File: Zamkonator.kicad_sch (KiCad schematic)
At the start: 27 parts, among them J1 Screw_Terminal_01x06, J3 Conn_01x08_Male, J4 Conn_02x06_Counter_Clockwise, J5 Conn_01x04_Female, J6 Conn_01x03_Female

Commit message: Switch to LCSC RJ45 socket
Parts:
- J1: LCSC (none) -> C918124
- J_LATCH1: LCSC (none) -> C918120
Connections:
- net RT9400_VA1: no longer J5.1 (Pin_1)
- net RT9400_VA2: no longer J5.2 (Pin_2)
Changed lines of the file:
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@@
-    (effects (font (size 1.27 1.27)) (justify right bottom))
-  )
-  (label "RT9400_VA2" (at 73.025 40.64 270)
     (effects (font (size 1.27 1.27)) (justify right bottom))
   )
   (label "RT9400_VA2" (at 110.49 73.66 90)
     (effects (font (size 1.27 1.27)) (justify left bottom))
-  )
-  (label "RT9400_VA1" (at 70.485 40.64 270)
-    (effects (font (size 1.27 1.27)) (justify right bottom))
   )
   (label "RT9400_VA1" (at 107.315 73.66 90)
@@
     )
     (property "Datasheet" "~" (id 3) (at 252.73 85.09 0)
+      (effects (font (size 1.27 1.27)) hide)
+    )
+    (property "LCSC" "C918124" (id 4) (at 252.73 85.09 0)
       (effects (font (size 1.27 1.27)) hide)
     )
@@
     )
     (property "Datasheet" "~" (id 3) (at 267.335 117.475 0)
+      (effects (font (size 1.27 1.27)) hide)
+    )
+    (property "LCSC" "C918120" (id 4) (at 267.335 117.475 0)
       (effects (font (size 1.27 1.27)) hide)
     )
@@
       (reference "#PWR07") (unit 1) (value "GND") (footprint "")
     )
-    (path "/0599421a-f0cb-4879-9da8-2ed04adba3ce/7d1d7dcf-40bf-4138-bc11-333a7bcfd3c6"
-      (reference "#PWR08") (unit 1) (value "GND") (footprint "")
-    )
     (path "/0599421a-f0cb-4879-9da8-2ed04adba3ce/61eecf11-6b4c-4999-be36-ff14b471e153"
       (reference "#PWR09") (unit 1) (value "+3V3") (footprint "")
@@
       (reference "#PWR010") (unit 1) (value "GND") (footprint "")
     )
-    (path "/0599421a-f0cb-4879-9da8-2ed04adba3ce/d1abf236-b779-413e-bcd6-7af093d733f0"
-      (reference "#PWR011") (unit 1) (value "GND") (footprint "")
-    )
     (path "/0599421a-f0cb-4879-9da8-2ed04adba3ce/c8cee972-1510-4b7d-b50a-8bda6d429ebd"
       (reference "#PWR012") (unit 1) (value "GND") (footprint "")
@@
       (reference "#PWR070") (unit 1) (value "GND") (footprint "")
     )
-    (path "/0599421a-f0cb-4879-9da8-2ed04adba3ce/94eb4dfe-898e-4163-9aef-43fee180666d"
-      (reference "#PWR071") (unit 1) (value "GND") (footprint "")
-    )
     (path "/8f150270-d3cb-4860-9563-91fde445dae8"
       (reference "#PWR0101") (unit 1) (value "+3.3V") (footprint "")
@@
       (reference "#PWR0109") (unit 1) (value "+3.3V") (footprint "")
     )
+    (path "/0599421a-f0cb-4879-9da8-2ed04adba3ce/6b65041a-d462-4dbd-9e89-0653ccb6d431"
+      (reference "#PWR0110") (unit 1) (value "GND") (footprint "")
+    )
     (path "/0599421a-f0cb-4879-9da8-2ed04adba3ce/b023df16-89a0-44f8-b620-c618db9e4a0e"
       (reference "C1") (unit 1) (value "47u") (footprint "Capacitor_SMD:C_0603_1608Metric_Pad1.08x0.95mm_HandSolder")
@@
       (reference "C36") (unit 1) (value "100n") (footprint "Capacitor_SMD:C_0603_1608Metric_Pad1.08x0.95mm_HandSolder")
     )
-    (path "/0599421a-f0cb-4879-9da8-2ed04adba3ce/71bbbb3a-cb3b-4a37-9c57-1f3f3d12232e"
-      (reference "C37") (unit 1) (value "100n") (footprint "Capacitor_SMD:C_0603_1608Metric_Pad1.08x0.95mm_HandSolder")
-    )
     (path "/0599421a-f0cb-4879-9da8-2ed04adba3ce/d0442497-8589-47ab-9e3c-70d05df16f8e"
       (reference "D1") (unit 1) (value "SM03") (footprint "Package_TO_SOT_SMD:TSOT-23_HandSoldering")
@@
       (reference "J1") (unit 1) (value "Screw_Terminal_01x06") (footprint "TerminalBlock_Phoenix:TerminalBlock_Phoenix_MPT-0,5-6-2.54_1x06_P2.54mm_Horizontal")
     )
-    (path "/0599421a-f0cb-4879-9da8-2ed04adba3ce/c0a1c66c-de6c-4624-85a0-87f1985b8000"
-      (reference "J2") (unit 1) (value "RJ45_Abracon_ARJP11A-MASA-B-A-EMU2") (footprint "Connector_RJ:RJ45_Abracon_ARJP11A-MA_Horizontal")
-    )
     (path "/ae3c1ce2-d60d-4c32-b4eb-1dde79f4bdfe"
       (reference "J3") (unit 1) (value "Conn_01x08_Male") (footprint "Connector_PinHeader_2.54mm:PinHeader_1x08_P2.54mm_Vertical")
@@
       (reference "R35") (unit 1) (value "DNP") (footprint "Resistor_SMD:R_0603_1608Metric_Pad0.98x0.95mm_HandSolder")
     )
+    (path "/0599421a-f0cb-4879-9da8-2ed04adba3ce/93d83c8f-5866-4858-88b3-ed62d232b59f"
+      (reference "RJ1") (unit 1) (value "HY931147C") (footprint "kicad_lceda:RJ45-TH_HY931147C")
+    )
     (path "/0dd39886-6ed0-43ed-af54-4a02cc0bde41/f7fe4e57-e013-4c02-a36f-5cbcf5aa62bd"

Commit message: Kicad updates, added missing resistances
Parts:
- J1: LCSC C918124 -> (none)
- J_LATCH1: LCSC C918120 -> (none)
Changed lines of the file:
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@@
-			)
-		)
-		(property "LCSC" "C918124"
-			(at 252.73 85.09 0)
-			(effects
-				(font
-					(size 1.27 1.27)
-				)
-				(hide yes)
 			)
 		)
@@
 			(at 267.335 117.475 0)
 			(effects
-				(font
-					(size 1.27 1.27)
-				)
-				(hide yes)
-			)
-		)
-		(property "LCSC" "C918120"
-			(at 267.335 117.475 0)
-			(effects

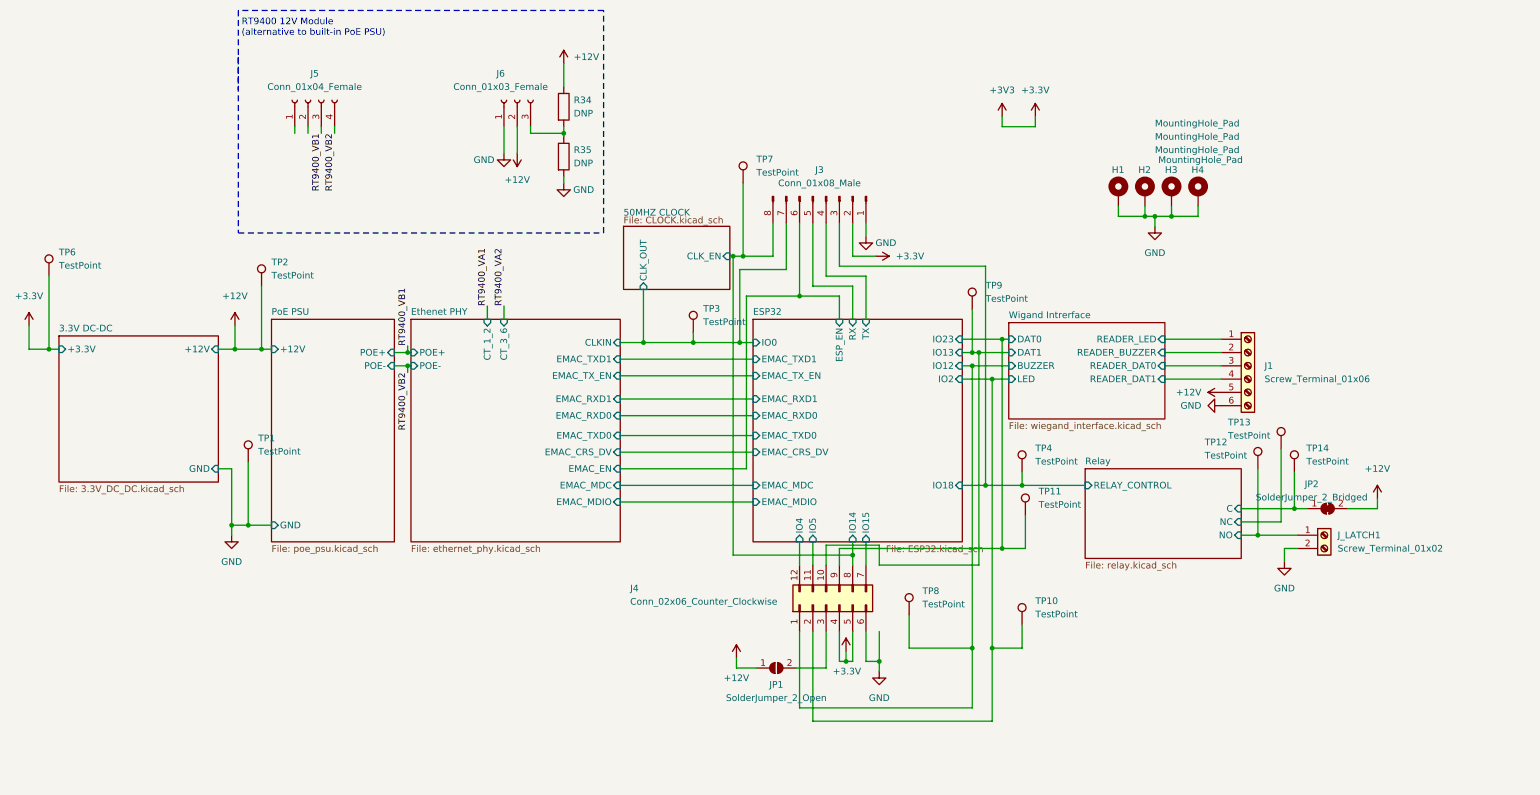
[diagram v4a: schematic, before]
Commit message: Update schematic for V1.1
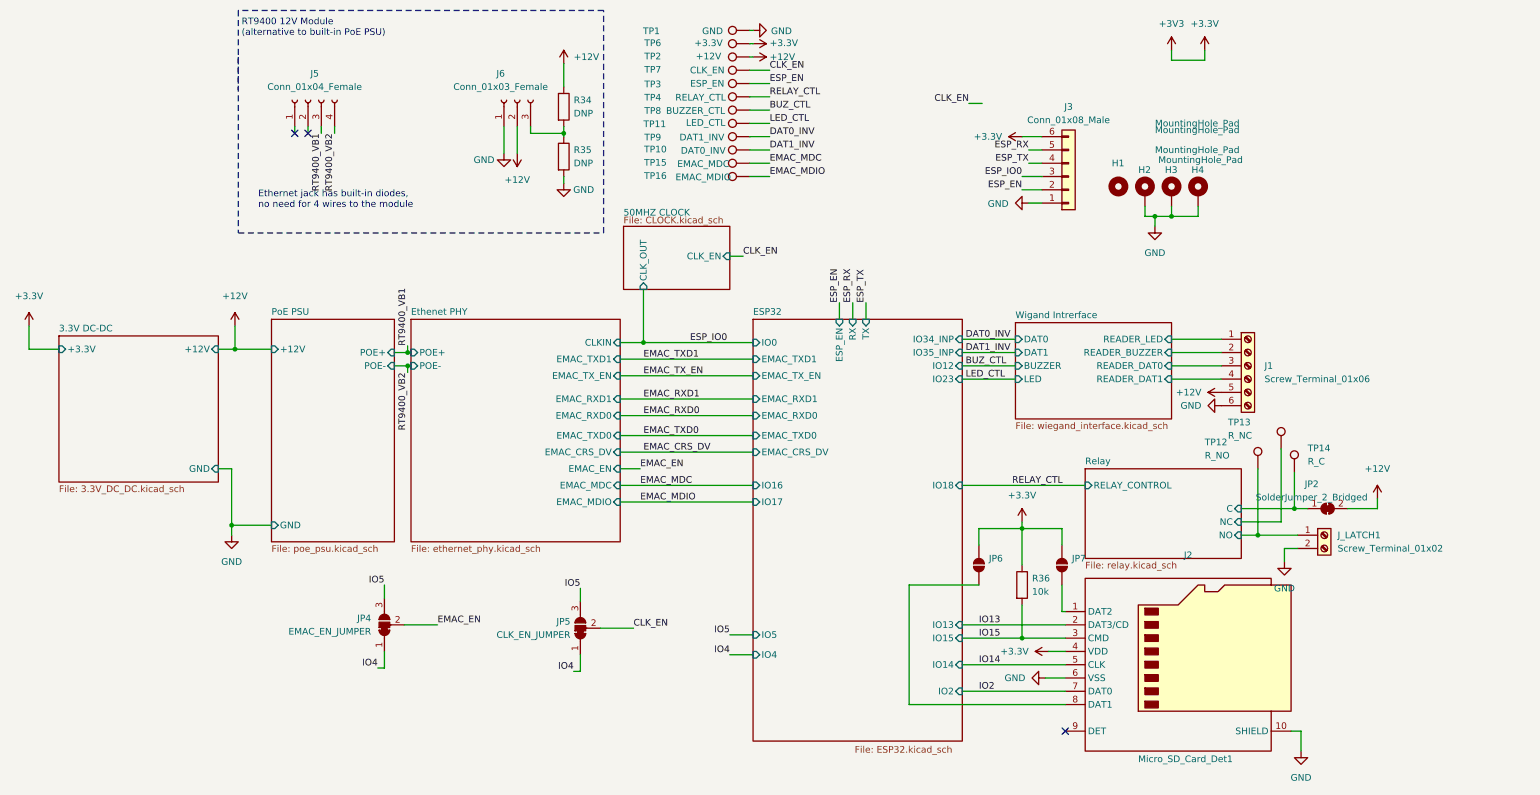
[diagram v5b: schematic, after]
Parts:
- removed J4: Conn_02x06_Counter_Clockwise, Connector_PinHeader_2.54mm:PinHeader_2x06_P2.54mm_Vertical, symbol Connector_Generic:Conn_02x06_Counter_Clockwise
- removed JP1: SolderJumper_2_Open, Jumper:SolderJumper-2_P1.3mm_Open_RoundedPad1.0x1.5mm, symbol Jumper:SolderJumper_2_Open
- added J2: Micro_SD_Card_Det1, Connector_Card:microSD_HC_Hirose_DM3AT-SF-PEJM5, symbol Connector:Micro_SD_Card_Det1
- added JP4: EMAC_EN_JUMPER, Jumper:SolderJumper-3_P1.3mm_Bridged12_RoundedPad1.0x1.5mm, symbol Jumper:SolderJumper_3_Bridged12
- added JP5: CLK_EN_JUMPER, Jumper:SolderJumper-3_P1.3mm_Bridged12_RoundedPad1.0x1.5mm, symbol Jumper:SolderJumper_3_Bridged12
- added JP6, JP7: SolderJumper_2_Open, Jumper:SolderJumper-2_P1.3mm_Open_RoundedPad1.0x1.5mm, symbol Jumper:SolderJumper_2_Open
- added R36: 10k, Resistor_SMD:R_0603_1608Metric_Pad0.98x0.95mm_HandSolder, symbol Device:R
- added TP15: EMAC_MDC, TestPoint:TestPoint_Pad_D1.5mm, symbol Connector:TestPoint
- added TP16: EMAC_MDIO, TestPoint:TestPoint_Pad_D1.5mm, symbol Connector:TestPoint
- H1: footprint MountingHole:MountingHole_3.2mm_M3_Pad_Via -> MountingHole:MountingHole_3.2mm_M3; symbol Mechanical:MountingHole_Pad -> Mechanical:MountingHole; now left out of the parts list
- J3: footprint Connector_PinHeader_2.54mm:PinHeader_1x08_P2.54mm_Vertical -> Connector_PinHeader_2.54mm:PinHeader_1x06_P2.54mm_Vertical; symbol Connector:Conn_01x08_Male -> Connector_Generic:Conn_01x06
- TP1: value TestPoint -> GND
- TP10: value TestPoint -> DAT0_INV
- TP11: value TestPoint -> LED_CTL
- TP12: value TestPoint -> R_NO
- TP13: value TestPoint -> R_NC
- TP14: value TestPoint -> R_C
- TP2: value TestPoint -> +12V
- TP3: value TestPoint -> ESP_EN
- TP4: value TestPoint -> RELAY_CTL
- TP6: value TestPoint -> +3.3V
- TP7: value TestPoint -> CLK_EN
- TP8: value TestPoint -> BUZZER_CTL
- TP9: value TestPoint -> DAT1_INV
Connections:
- net ESP32/ESP_EN is gone; now on net +3.3V: J3.6 (Pin_6)
- net +3.3V: now also J2.4 (VDD), JP6.2 (B), JP7.2 (B), R36.1; no longer J3.2 (Pin_2)
- net GND: now also J2.10 (SHIELD), J2.6 (VSS); no longer H1.1
- net 50MHZ CLOCK/CLK_EN renamed CLK_EN
- net CLK_EN: now also JP5.2 (C); no longer J3.8 (Pin_8)
- net 50MHZ CLOCK/CLK_OUT renamed ESP_EN
- net ESP_EN: now also J3.2 (Pin_2); no longer J3.7 (Pin_7)
- net ESP32/IO12 renamed BUZ_CTL
- net ESP32/IO13 renamed DAT0_INV
- net ESP32/IO18 renamed ESP_IO0
- net ESP_IO0: no longer TP4.1
- net ESP32/IO2 renamed DAT1_INV
- net ESP32/IO23 renamed LED_CTL
- net ESP32/RX renamed ESP_RX
- net ESP32/TX renamed ESP_TX
- new net: J2.8 (DAT1), JP6.1 (A)
- new net: J2.1 (DAT2), JP7.1 (A)
- new net EMAC_EN: JP4.2 (C)
- new net EMAC_MDC: TP15.1
- new net EMAC_MDIO: TP16.1
- new net IO13: J2.2 (DAT3/CD)
- new net IO14: J2.5 (CLK)
- new net IO15: J2.3 (CMD), R36.2
- new net IO2: J2.7 (DAT0)
- new net IO4: JP4.1 (A), JP5.1 (A)
- new net IO5: JP4.3 (B), JP5.3 (B)
- new net RELAY_CTL: TP4.1
- no-connect marks 0 -> 3
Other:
- sheet ESP32 ports: added IO16, IO17, IO34_INP, IO35_INP; removed EMAC_MDC, EMAC_MDIO
- sheet Ethenet PHY ports: added none; removed CT_1_2, CT_3_6
- note added: "Ethernet jack has built-in diodes, no need for 4 wires to the module"
- moved on the sheet: TP7, TP8, TP9

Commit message: BOM updates & schematic fixes
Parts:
- TP1, TP10, TP11, TP15, TP16, TP2, TP3, TP4, TP6, TP7, TP8, TP9: now left out of the parts list

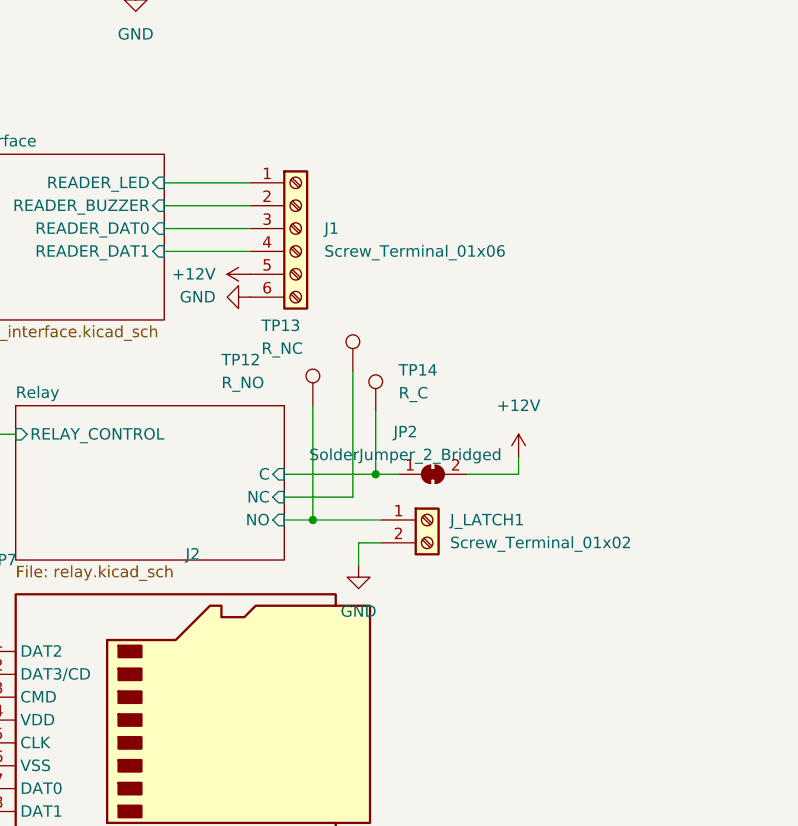
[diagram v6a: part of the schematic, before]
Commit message: fix PoE transofrmer polarity, add more relay outputs
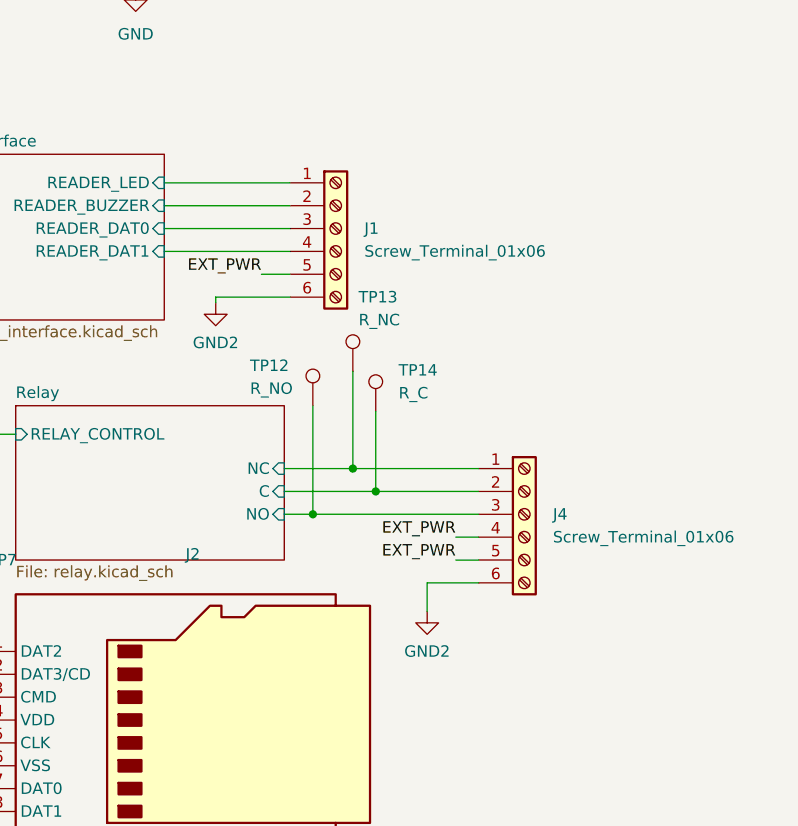
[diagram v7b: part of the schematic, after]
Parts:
- removed JP2: SolderJumper_2_Bridged, Jumper:SolderJumper-2_P1.3mm_Bridged_RoundedPad1.0x1.5mm, symbol Jumper:SolderJumper_2_Bridged
- removed J_LATCH1: Screw_Terminal_01x02, TerminalBlock_Phoenix:TerminalBlock_Phoenix_MPT-0,5-2-2.54_1x02_P2.54mm_Horizontal, symbol Connector:Screw_Terminal_01x02
- added J4: Screw_Terminal_01x06, TerminalBlock_Phoenix:TerminalBlock_Phoenix_MPT-0,5-6-2.54_1x06_P2.54mm_Horizontal, symbol Connector:Screw_Terminal_01x06
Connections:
- net +12V: no longer J1.5 (Pin_5)
- net GND: no longer J1.6 (Pin_6)
- net Relay/C: now also J4.2 (Pin_2)
- net Relay/NC: now also J4.1 (Pin_1)
- net Relay/NO: now also J4.3 (Pin_3)
- new net EXT_PWR: J1.5 (Pin_5), J4.4 (Pin_4), J4.5 (Pin_5)
- new net GND2: J1.6 (Pin_6), J4.6 (Pin_6)
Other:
- moved on the sheet: J1

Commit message: DO the bulk of rev 1.2 layout
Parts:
- removed JP4: EMAC_EN_JUMPER, Jumper:SolderJumper-3_P1.3mm_Bridged12_RoundedPad1.0x1.5mm, symbol Jumper:SolderJumper_3_Bridged12
- removed JP5: CLK_EN_JUMPER, Jumper:SolderJumper-3_P1.3mm_Bridged12_RoundedPad1.0x1.5mm, symbol Jumper:SolderJumper_3_Bridged12
- added D13: PESD15VL1BA, Diode_SMD:D_SOD-323, symbol Device:D_TVS
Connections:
- net EXT_PWR: now also D13.2 (A2)
- net GND: no longer H4.1
- net GND2: now also H4.1, D13.1 (A1)
- net Relay/C: now also J4.3 (Pin_3); no longer J4.2 (Pin_2)
- net Relay/NO: now also J4.2 (Pin_2); no longer J4.3 (Pin_3)
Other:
- moved on the sheet: H4, TP12, TP14
